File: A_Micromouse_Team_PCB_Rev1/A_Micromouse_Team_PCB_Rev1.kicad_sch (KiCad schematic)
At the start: 10 parts, among them J1 Conn_01x07_Pin, J2 Conn_01x07_Pin, J3 Conn_01x07_Pin, J4 Conn_01x07_Pin, J5 Conn_01x06_Pin, J6 Conn_01x06_Pin, J8 Conn_01x07_Pin, U2 BNO055, U3 TB6612FNG, U4 TinyPico_V3

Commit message: second commit
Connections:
- net +5V: no longer J1.3 (Pin_3), J2.3 (Pin_3), J3.3 (Pin_3), J4.3 (Pin_3), J8.3 (Pin_3)
- net at U3.1 (AO1), U3.2 (AO1): no longer J6.6 (Pin_6)
- net at U3.11 (BO1), U3.12 (BO1): no longer J5.6 (Pin_6)
- net at U3.5 (AO2), U3.6 (AO2): no longer J6.5 (Pin_5)
- net at U3.7 (BO2), U3.8 (BO2): no longer J5.5 (Pin_5)
- net at U4.10 (IO25): now also J4.6 (Pin_6)
- net at U4.13 (IO33): no longer J6.3 (Pin_3)
- net at U4.14 (IO32): no longer J6.2 (Pin_2)
- net at U4.17 (SS): no longer J5.3 (Pin_3)
- net at U4.18 (SCK): no longer J5.2 (Pin_2)
- net at U4.7 (IO15): now also J1.6 (Pin_6)
- net at U4.8 (IO27): now also J2.6 (Pin_6)
- net at U4.9 (IO26): now also J3.6 (Pin_6)
- removed net GPIO: J1.6 (Pin_6), J2.6 (Pin_6), J3.6 (Pin_6), J4.6 (Pin_6), J8.6 (Pin_6), U4.6 (IO14)
- new net: J8.6 (Pin_6), U4.6 (IO14)
- new net GND1: J1.3 (Pin_3), J2.3 (Pin_3), J3.3 (Pin_3), J4.3 (Pin_3), J8.3 (Pin_3)

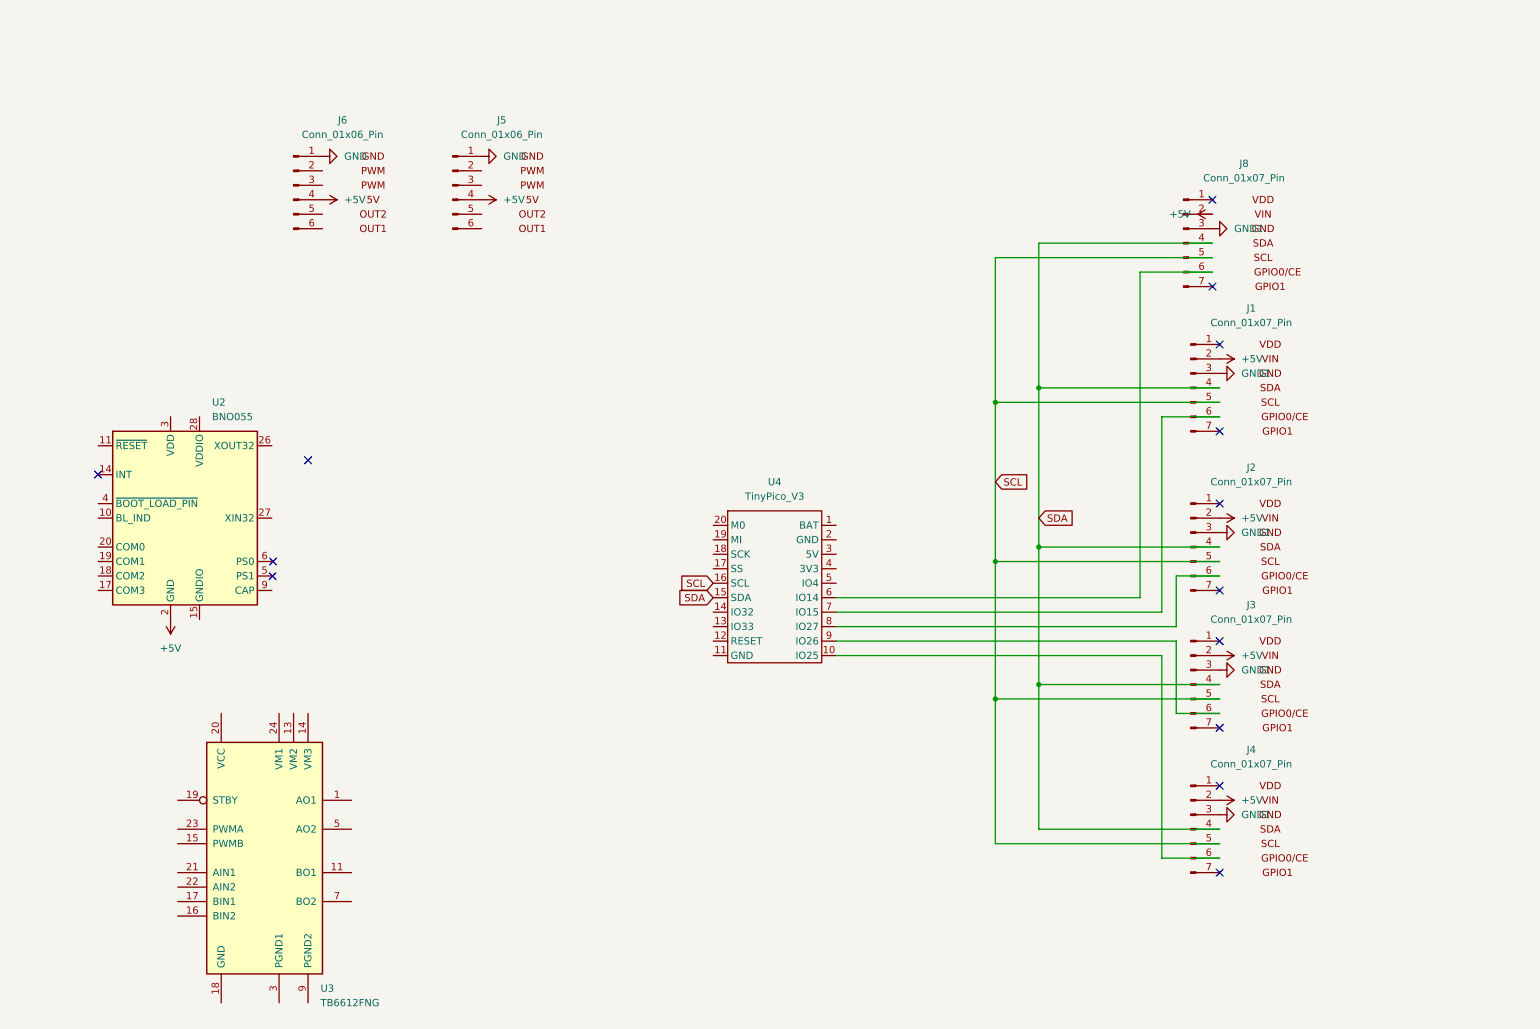
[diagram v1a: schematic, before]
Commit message: updated schematic with teensy
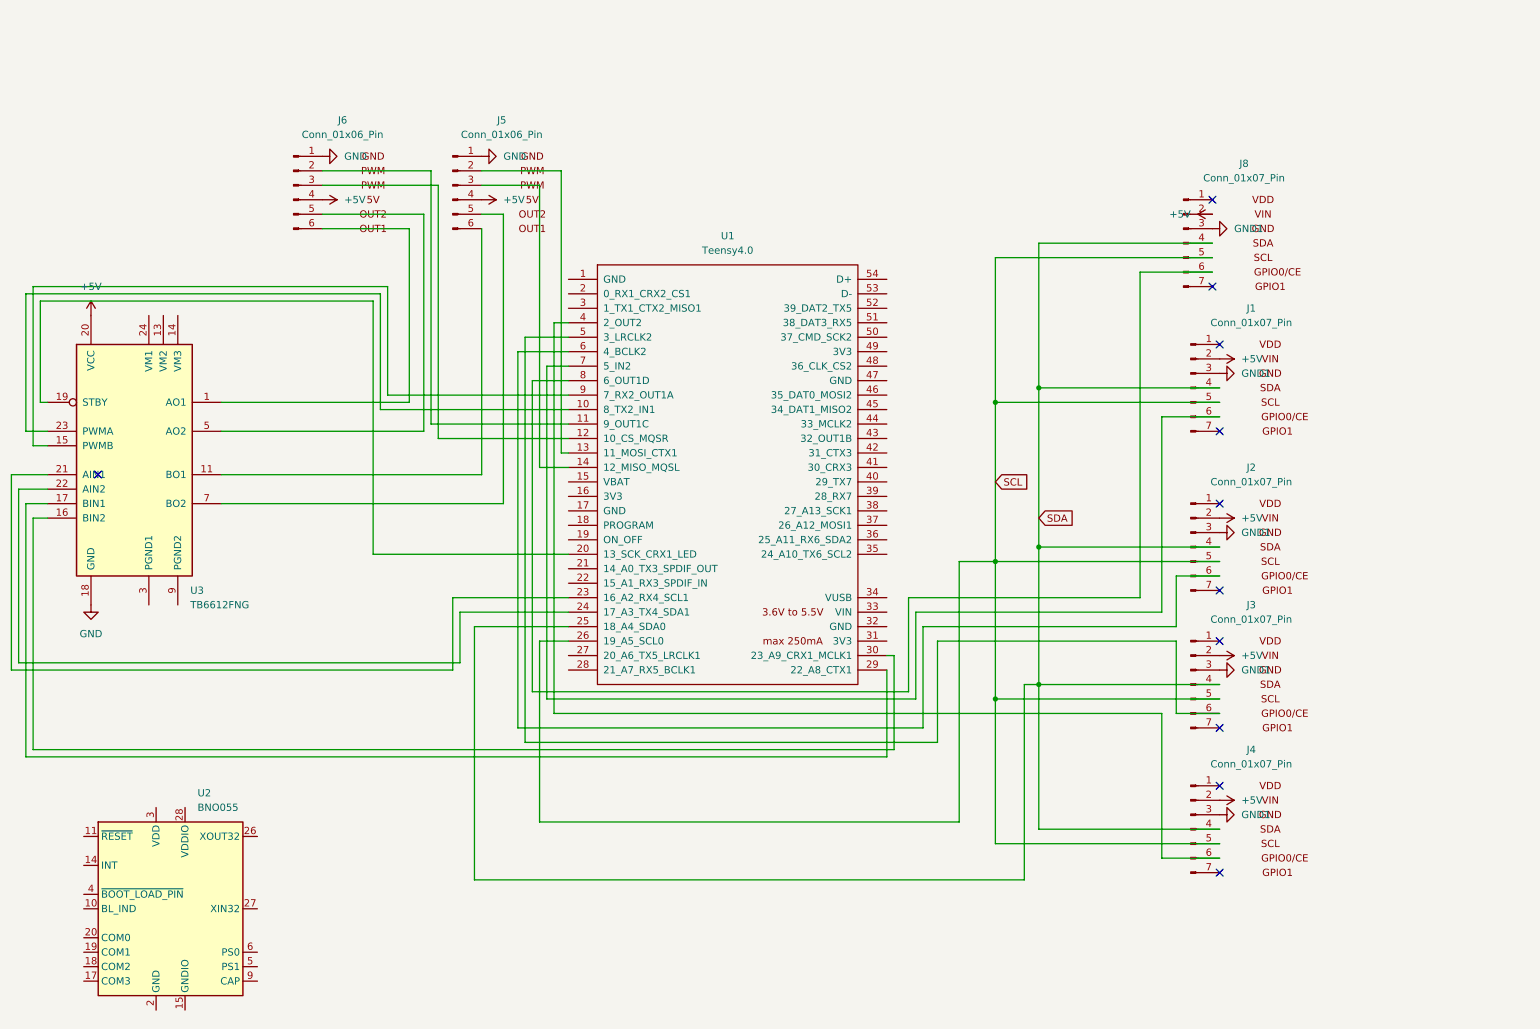
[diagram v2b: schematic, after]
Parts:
- removed U4: TinyPico_V3, Assorted_Footprints:TinyPICO_Nano, symbol MicromouseSymbolLibrary:TinyPico_V3
- added U1: Teensy4.0, Teensy4.0:Teensy40, symbol teensy:Teensy4.0
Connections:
- net +5V: now also U3.20 (VCC); no longer U2.2 (GND)
- net GND: now also U3.18 (GND)
- net SCL: now also U1.26 (19_A5_SCL0)
- net SDA: now also U1.25 (18_A4_SDA0)
- net at U3.1 (AO1), U3.2 (AO1): now also J6.6 (Pin_6)
- net at U3.11 (BO1), U3.12 (BO1): now also J5.6 (Pin_6)
- net at U3.15 (PWMB): now also U1.9 (7_RX2_OUT1A)
- net at U3.16 (BIN2): now also U1.30 (23_A9_CRX1_MCLK1)
- net at U3.17 (BIN1): now also U1.29 (22_A8_CTX1)
- net at U3.19 (STBY): now also U1.20 (13_SCK_CRX1_LED)
- net at U3.21 (AIN1): now also U1.23 (16_A2_RX4_SCL1)
- net at U3.22 (AIN2): now also U1.24 (17_A3_TX4_SDA1)
- net at U3.23 (PWMA): now also U1.10 (8_TX2_IN1)
- net at U3.5 (AO2), U3.6 (AO2): now also J6.5 (Pin_5)
- net at U3.7 (BO2), U3.8 (BO2): now also J5.5 (Pin_5)
- net at J3.6 (Pin_6): now also U1.5 (3_LRCLK2)
- net at J8.6 (Pin_6): now also U1.8 (6_OUT1D)
- net at J4.6 (Pin_6): now also U1.4 (2_OUT2)
- net at J1.6 (Pin_6): now also U1.7 (5_IN2)
- net at J2.6 (Pin_6): now also U1.6 (4_BCLK2)
- net at J5.2 (Pin_2): now also U1.13 (11_MOSI_CTX1)
- net at J5.3 (Pin_3): now also U1.14 (12_MISO_MQSL)
- net at J6.2 (Pin_2): now also U1.11 (9_OUT1C)
- net at J6.3 (Pin_3): now also U1.12 (10_CS_MQSR)
- no-connect marks 14 -> 11
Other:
- moved on the sheet: U2, U3

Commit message: changed Net Classes
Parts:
- added J10: Conn_01x06, Connector_PinHeader_2.00mm:PinHeader_1x06_P2.00mm_Vertical, symbol Connector_Generic:Conn_01x06
- added J7: Conn_01x04_Socket, Connector_PinHeader_2.00mm:PinHeader_1x04_P2.00mm_Vertical, symbol Connector:Conn_01x04_Socket
- added J9: Conn_01x02_Socket, Connector_PinHeader_2.00mm:PinHeader_1x02_P2.00mm_Vertical, symbol Connector:Conn_01x02_Socket
- J4: footprint (none) -> Connector_PinHeader_2.54mm:PinHeader_1x07_P2.54mm_Vertical
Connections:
- net +5V: now also J10.4 (Pin_4), J10.5 (Pin_5), J7.3 (Pin_3), J9.1 (Pin_1)
- net GND: now also J10.2 (Pin_2), J10.3 (Pin_3), J7.1 (Pin_1), J7.4 (Pin_4), J9.2 (Pin_2)
- net +12V: now reaches U3.24 (VM1)
- net +12V: now also J10.1 (Pin_1)
- net at U1.22 (15_A1_RX3_SPDIF_IN): now also J7.2 (Pin_2)
- net at U1.52 (39_DAT2_TX5): now also J10.6 (Pin_6)
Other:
- moved on the sheet: U2

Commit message: fixed repo
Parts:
- added SW1: SW_DIP_x06, Package_DIP:DIP-12_W7.62mm, symbol Switch:SW_DIP_x06
- J1: value Conn_01x07_Pin -> TOF2
- J10: value Conn_01x06 -> 5V->12V; footprint Connector_PinHeader_2.00mm:PinHeader_1x06_P2.00mm_Vertical -> Connector_PinHeader_2.54mm:PinHeader_1x06_P2.54mm_Vertical
- J2: value Conn_01x07_Pin -> TOF3
- J3: value Conn_01x07_Pin -> TOF4
- J4: value Conn_01x07_Pin -> TOF5
- J5: value Conn_01x06_Pin -> Motor1
- J6: value Conn_01x06_Pin -> Motor2
- J7: value Conn_01x04_Socket -> NeoPixel; footprint Connector_PinHeader_2.00mm:PinHeader_1x04_P2.00mm_Vertical -> Connector_PinHeader_2.54mm:PinHeader_1x04_P2.54mm_Vertical
- J8: value Conn_01x07_Pin -> TOF1
- J9: value Conn_01x02_Socket -> Battery
- U1: footprint Teensy4.0:Teensy40 -> MicromouseLibaryNew:Teensy40
- U2: value BNO055 -> IMU; footprint Package_LGA:LGA-28_5.2x3.8mm_P0.5mm -> MicromouseLibaryNew:MODULE_4754
- U3: value TB6612FNG -> MotorController; footprint Package_SO:SSOP-24_5.3x8.2mm_P0.65mm -> MicromouseLibaryNew:MotorController
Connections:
- net +12V: now also SW1.11; no longer U3.24 (VM1)
- net +5V: now also SW1.12; no longer J9.1 (Pin_1)
- net GND: now also U1.1 (GND), U2.2 (GND)
- net at U3.16 (BIN2): now also U2.19 (COM1); no longer U1.30 (23_A9_CRX1_MCLK1)
- net at U3.22 (AIN2): now also U2.14 (INT); no longer U1.24 (17_A3_TX4_SDA1)
- net at J10.6 (Pin_6): now also U1.28 (21_A7_RX5_BCLK1); no longer U1.52 (39_DAT2_TX5)
- net at U2.13 (PIN13): now also U1.24 (17_A3_TX4_SDA1)
- net at U2.6 (PS0): now also U1.30 (23_A9_CRX1_MCLK1)
- net at U1.27 (20_A6_TX5_LRCLK1): now also SW1.3
- new net: J9.1 (Pin_1), SW1.1
- new net: SW1.2, U3.24 (VM1)
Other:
- moved on the sheet: J10, U2

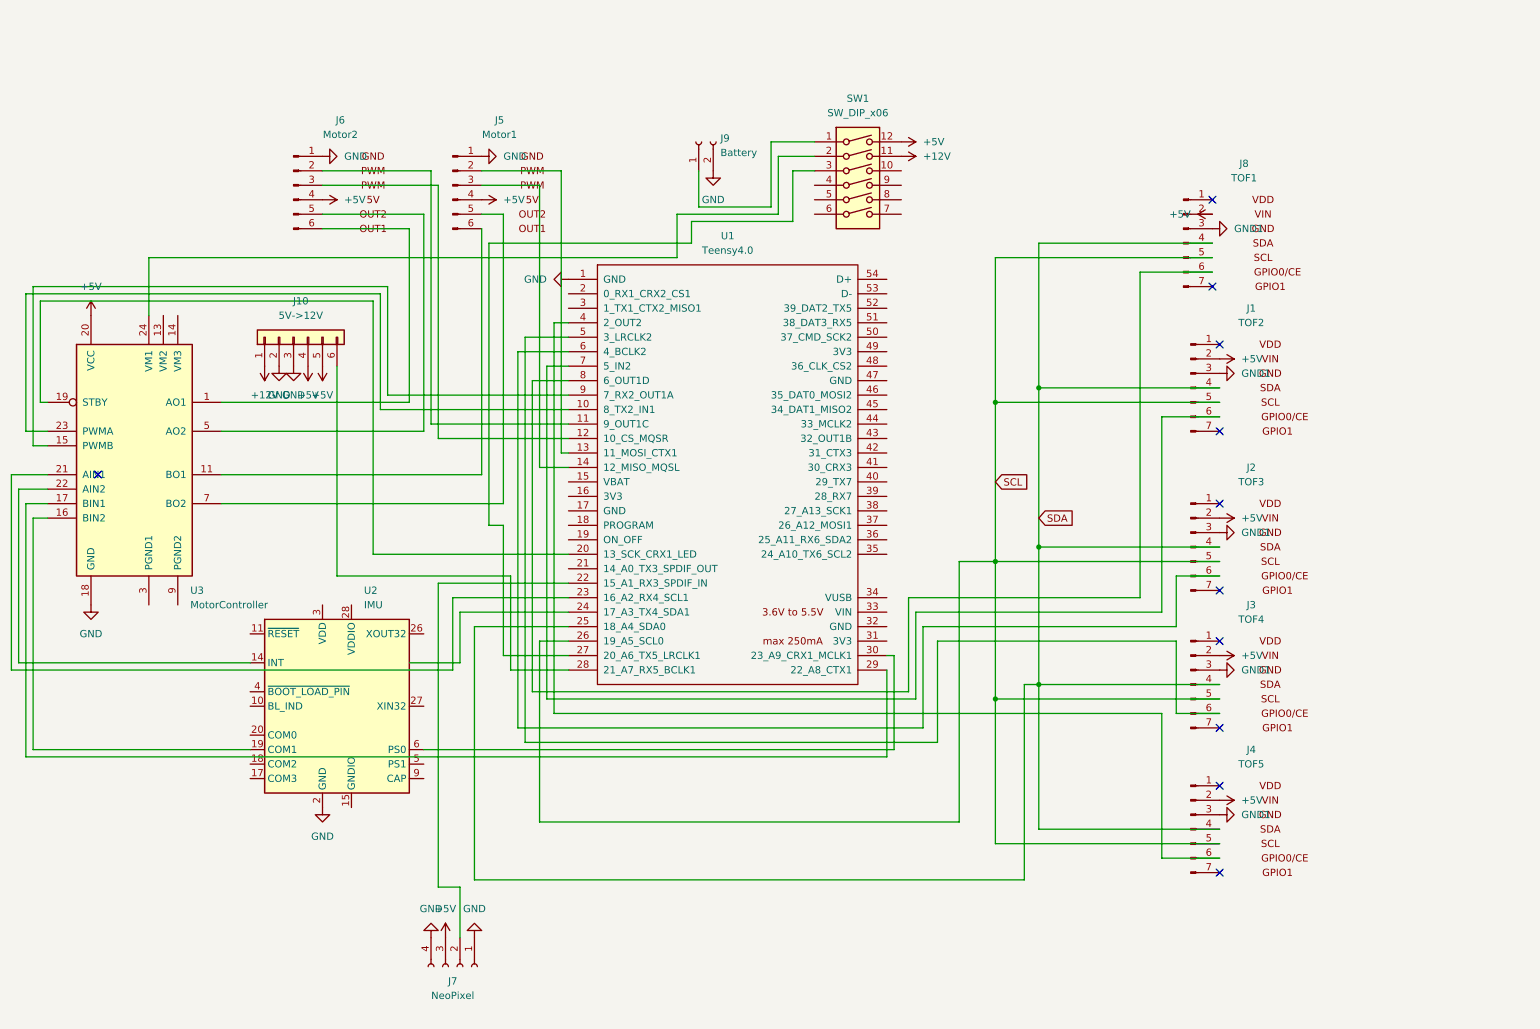
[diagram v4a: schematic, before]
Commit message: rearranged schematic to make more legible
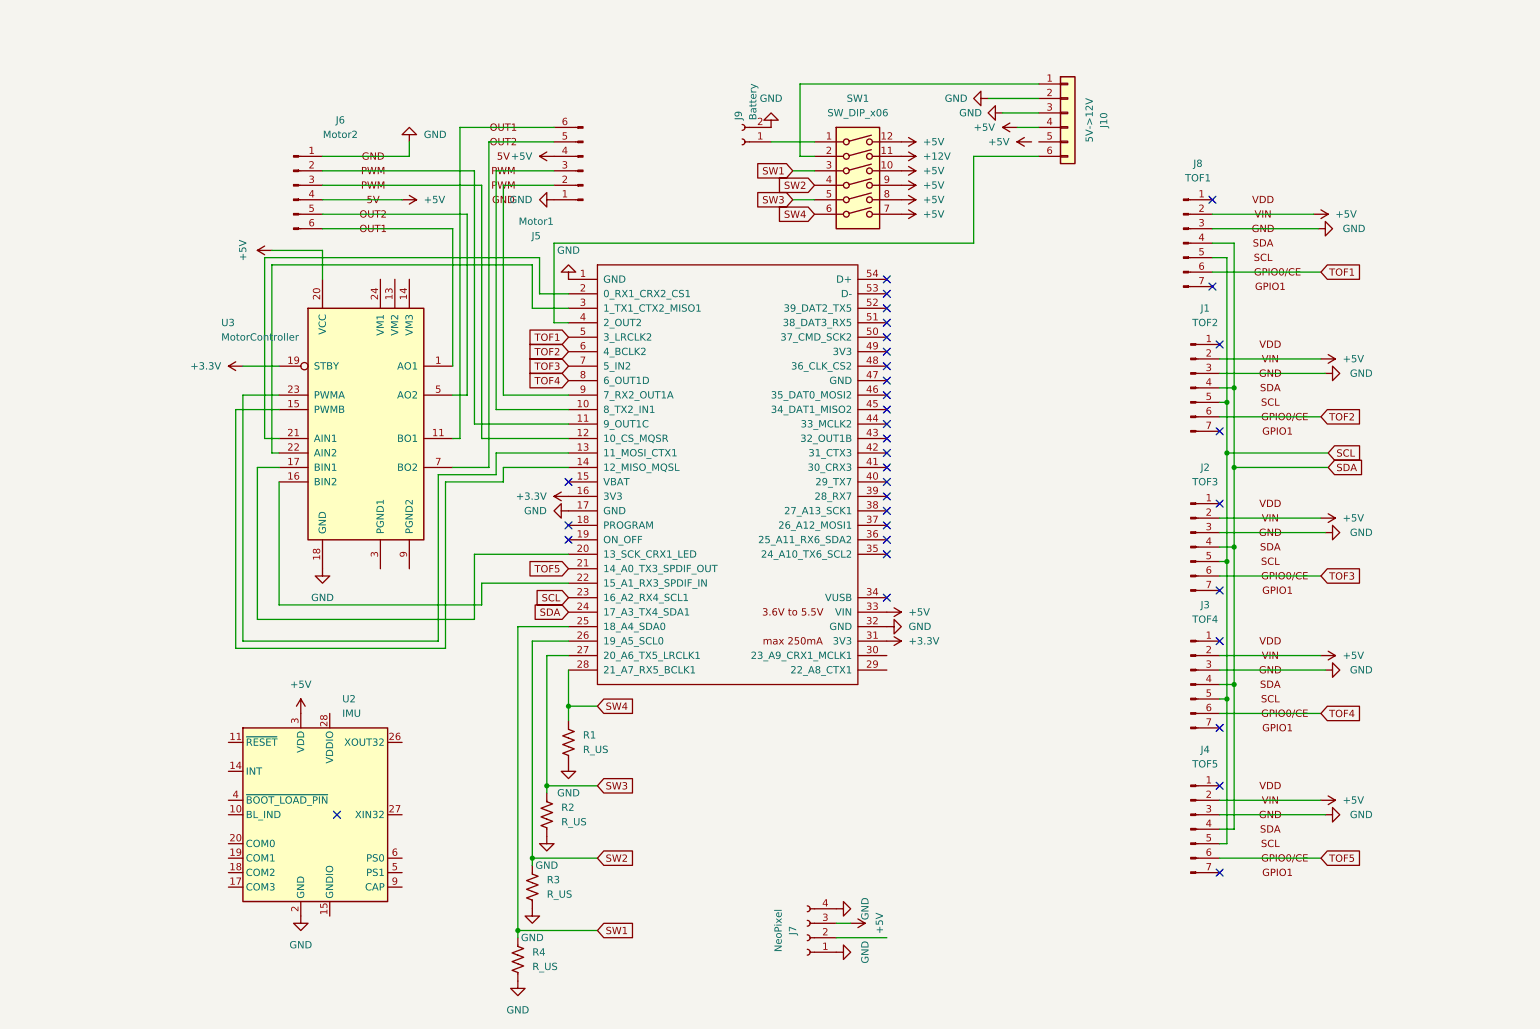
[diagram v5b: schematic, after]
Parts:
- added R1, R2, R3, R4: R_US, symbol Device:R_US
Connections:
- net GND1 is gone; now on net GND: J1.3 (Pin_3), J2.3 (Pin_3), J3.3 (Pin_3), J4.3 (Pin_3), J8.3 (Pin_3)
- net +12V: no longer J10.1 (Pin_1)
- net +5V: now also SW1.10, SW1.7, SW1.8, SW1.9, U1.33 (VIN), U2.3 (VDD); no longer J10.5 (Pin_5)
- net GND: now also U1.17 (GND), U1.32 (GND), R1.2, R2.2, R3.2, R4.2
- net SCL: now also U1.23 (16_A2_RX4_SCL1); no longer U1.26 (19_A5_SCL0)
- net SDA: now also U1.24 (17_A3_TX4_SDA1); no longer U1.25 (18_A4_SDA0)
- net at U3.15 (PWMB): now also U1.14 (12_MISO_MQSL); no longer U1.9 (7_RX2_OUT1A)
- net at U3.16 (BIN2): now also U1.22 (15_A1_RX3_SPDIF_IN); no longer U2.19 (COM1)
- net at U3.17 (BIN1): now also U1.20 (13_SCK_CRX1_LED); no longer U1.29 (22_A8_CTX1)
- net +3.3V: now reaches U3.19 (STBY)
- net +3.3V: now also U1.16 (3V3), U1.31 (3V3); no longer U1.20 (13_SCK_CRX1_LED)
- net at U3.21 (AIN1): now also U1.2 (0_RX1_CRX2_CS1); no longer U1.23 (16_A2_RX4_SCL1)
- net at U3.22 (AIN2): now also U1.3 (1_TX1_CTX2_MISO1); no longer U2.14 (INT)
- net at U3.23 (PWMA): now also U1.13 (11_MOSI_CTX1); no longer U1.10 (8_TX2_IN1)
- net at U3.24 (VM1): no longer SW1.2
- net at J10.6 (Pin_6): now also U1.4 (2_OUT2); no longer U1.28 (21_A7_RX5_BCLK1)
- net at U2.13 (PIN13): no longer U1.24 (17_A3_TX4_SDA1)
- net at U2.6 (PS0): no longer U1.30 (23_A9_CRX1_MCLK1)
- net TOF1: now reaches U1.5 (3_LRCLK2)
- net TOF1: now also J8.6 (Pin_6); no longer J3.6 (Pin_6)
- net at J7.2 (Pin_2): no longer U1.22 (15_A1_RX3_SPDIF_IN)
- net TOF4: now reaches U1.8 (6_OUT1D)
- net TOF4: now also J3.6 (Pin_6); no longer J8.6 (Pin_6)
- net TOF2: now reaches U1.6 (4_BCLK2)
- net TOF2: now also J1.6 (Pin_6); no longer J2.6 (Pin_6)
- net at J5.2 (Pin_2): now also U1.9 (7_RX2_OUT1A); no longer U1.13 (11_MOSI_CTX1)
- net at J5.3 (Pin_3): now also U1.10 (8_TX2_IN1); no longer U1.14 (12_MISO_MQSL)
- net TOF3: now reaches U1.7 (5_IN2)
- net TOF3: now also J2.6 (Pin_6); no longer J1.6 (Pin_6)
- net TOF5: now reaches J4.6 (Pin_6)
- net TOF5: now also U1.21 (14_A0_TX3_SPDIF_OUT); no longer U1.4 (2_OUT2)
- net SW1: now reaches SW1.3
- net SW1: now also U1.25 (18_A4_SDA0), R4.1; no longer U1.27 (20_A6_TX5_LRCLK1)
- net SW2: now reaches SW1.4
- net SW2: now also U1.26 (19_A5_SCL0), R3.1
- net SW3: now reaches SW1.5
- net SW3: now also U1.27 (20_A6_TX5_LRCLK1), R2.1
- net SW4: now reaches SW1.6
- net SW4: now also U1.28 (21_A7_RX5_BCLK1), R1.1
- new net: J10.1 (Pin_1), SW1.2
- no-connect marks 11 -> 35
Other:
- moved on the sheet: J5, J7, J9, U2, U3
